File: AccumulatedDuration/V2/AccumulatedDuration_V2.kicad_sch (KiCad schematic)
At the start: 4 parts, among them J1 Conn_01x02_Socket, J1 Conn_01x04_Socket, J3 Conn_01x04_Socket

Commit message: * Release AccumulatedDuration v2 hardware.
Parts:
- added D1: 1N4001, Diode_THT:D_DO-41_SOD81_P10.16mm_Horizontal, symbol Diode:1N4001
- added J2: Conn_01x03_Socket, symbol Connector:Conn_01x03_Socket
- added J5: Conn_01x04_Socket, symbol Connector:Conn_01x04_Socket
- added K1: G5NB-1A-E, Relay_THT:Relay_SPST_TE_PCH-1xxx2M, symbol Relay:TE_PCH-1xxx2M
- added R1: 82, symbol Device:R
- J3: value Conn_01x04_Socket -> 01x04_hold
- renumbered J1 to J4
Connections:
- net +12V: now also J4.4 (Pin_4), J2.3 (Pin_3); no longer J1.2 (Pin_2)
- net GND: now also A1.29 (GND), A1.4 (GND), J4.1 (Pin_1), J2.1 (Pin_1), J2.2 (Pin_2), J5.4 (Pin_4); no longer J1.1 (Pin_1)
- net RS485_A: now reaches J4.2 (Pin_2)
- net RS485_B: now reaches J4.3 (Pin_3)
- net RO: now reaches J3.1 (Pin_1)
- net RO: now also A1.8 (D5)
- net RE_NEG: now reaches J3.2 (Pin_2)
- net RE_NEG: now also A1.7 (D4)
- net DE: now reaches J3.3 (Pin_3)
- net DE: now also A1.6 (D3)
- net DI: now reaches J3.4 (Pin_4)
- net DI: now also A1.5 (D2)
- net LCD_SDA: now reaches A1.23 (A4)
- net LCD_SDA: now also J5.2 (Pin_2)
- net LCD_SCL: now reaches A1.24 (A5)
- net LCD_SCL: now also J5.3 (Pin_3)
- net +5V: now reaches A1.27 (+5V)
- net +5V: now also J5.1 (Pin_1), R1.1
- net at A1.9 (D6): now also D1.2 (A), K1.5
- new net: D1.1 (K), K1.1, R1.2
- new net: J1.2 (Pin_2), K1.2
- new net: J1.1 (Pin_1), K1.3
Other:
- moved on the sheet: A1, J3, J4

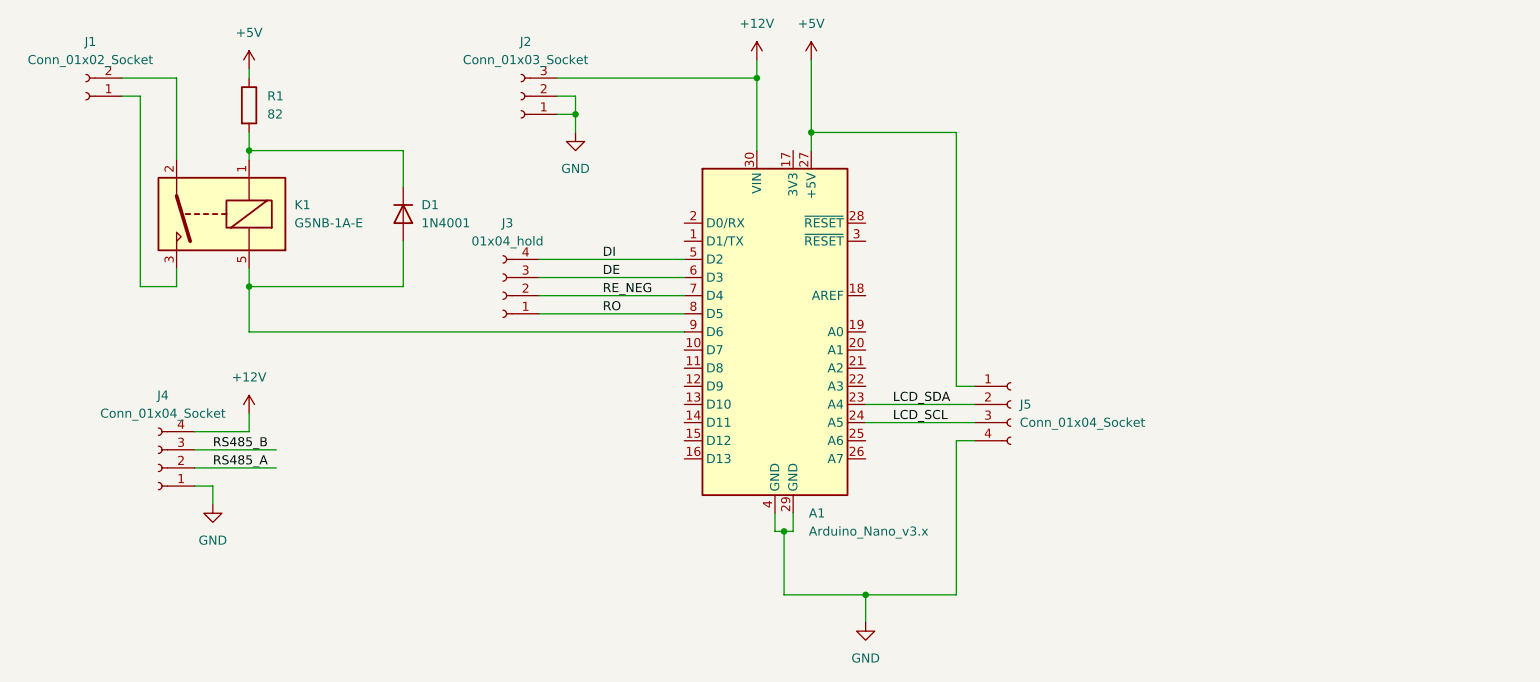
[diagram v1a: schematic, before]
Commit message: * Modify AccumulatedDuration V2 layout.
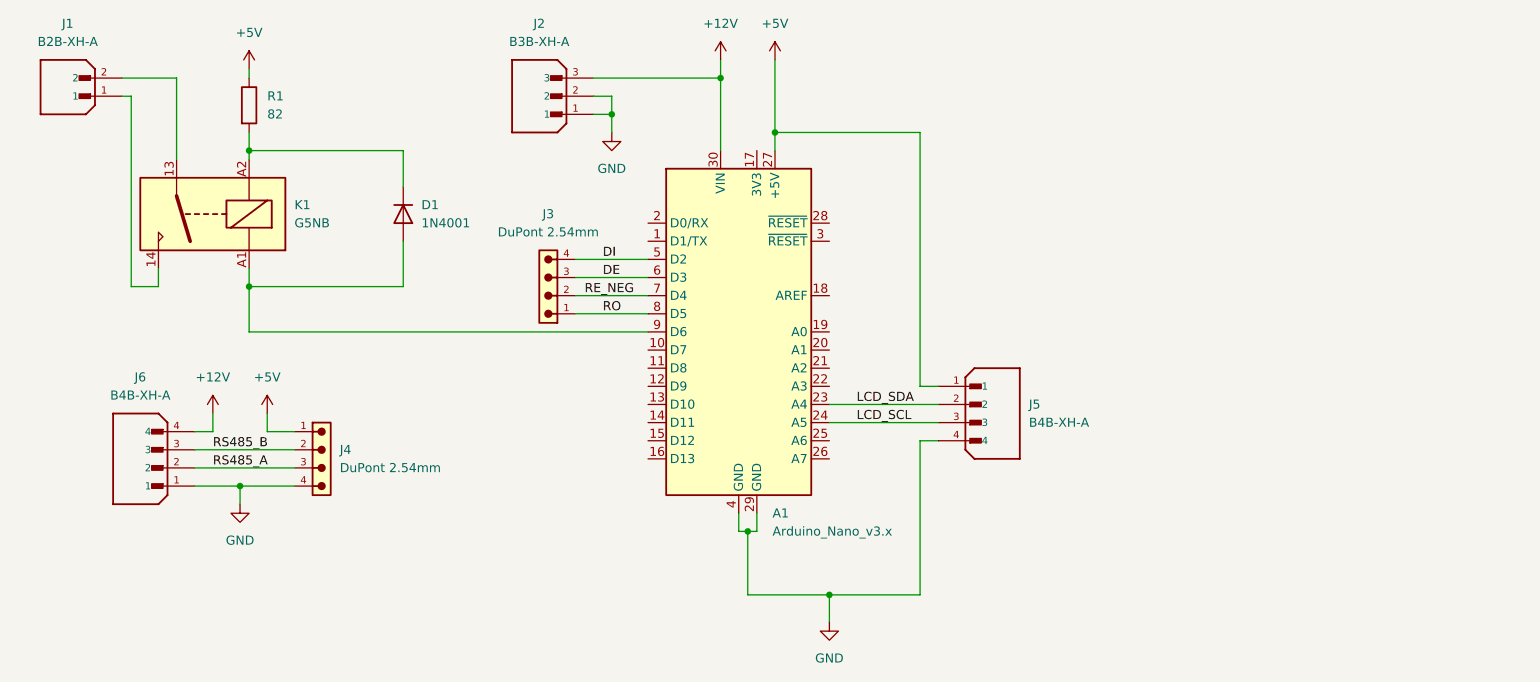
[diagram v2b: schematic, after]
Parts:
- removed J1: Conn_01x02_Socket, symbol Connector:Conn_01x02_Socket
- removed J2: Conn_01x03_Socket, symbol Connector:Conn_01x03_Socket
- removed J3: 01x04_hold, symbol Connector:Conn_01x04_Socket
- removed J4, J5: Conn_01x04_Socket, symbol Connector:Conn_01x04_Socket
- removed K1: G5NB-1A-E, Relay_THT:Relay_SPST_TE_PCH-1xxx2M, symbol Relay:TE_PCH-1xxx2M
- added J1: B2B-XH-A, B2B_XH_A:JST_B2B-XH-A, symbol B2B-XH-A:B2B-XH-A
- added J2: B3B-XH-A, B3B_XH_A:JST_B3B-XH-A, symbol B3B-XH-A:B3B-XH-A
- added J3, J4: DuPont 2.54mm, 61300411121:61300411121, symbol 6130XX11121_61300411121:6130XX11121_61300411121
- added J5, J6: B4B-XH-A, B4B_XH_A:JST_B4B-XH-A, symbol B4B-XH-A:B4B-XH-A
- added K1: G5NB, Relay_THT:Relay_SPST_Omron_G5NB, symbol Relay:G5NB
- R1: footprint (none) -> Resistor_THT:R_Axial_DIN0309_L9.0mm_D3.2mm_P12.70mm_Horizontal
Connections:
- net +12V: now also J2.3, J6.4
- net +5V: now also J4.1, J5.1
- net DE: now also J3.3
- net DI: now also J3.4
- net GND: now also J2.1, J2.2, J4.4, J5.4, J6.1
- net LCD_SCL: now also J5.3
- net LCD_SDA: now also J5.2
- net RE_NEG: now also J3.2
- net RO: now also J3.1
- net RS485_A: now also J4.3, J6.2
- net RS485_B: now also J4.2, J6.3
- net at D1.1 (K), R1.2: now also K1.A2
- net at A1.9 (D6), D1.2 (A): now also K1.A1
- new net: J1.1, K1.14
- new net: J1.2, K1.13
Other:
- moved on the sheet: A1
